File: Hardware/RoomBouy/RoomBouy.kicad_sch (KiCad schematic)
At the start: 30 parts, among them J1 Roomba Wake, J2 Raspberry_Pi_2_3, J3 Roomba Connector, J4 ProtoPad, J5 Servo, Q1 MMBT3904, Q2 MMBT3904, Q3 MMBT3906, Q4 MMBT3904, Q6 MMBT3906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

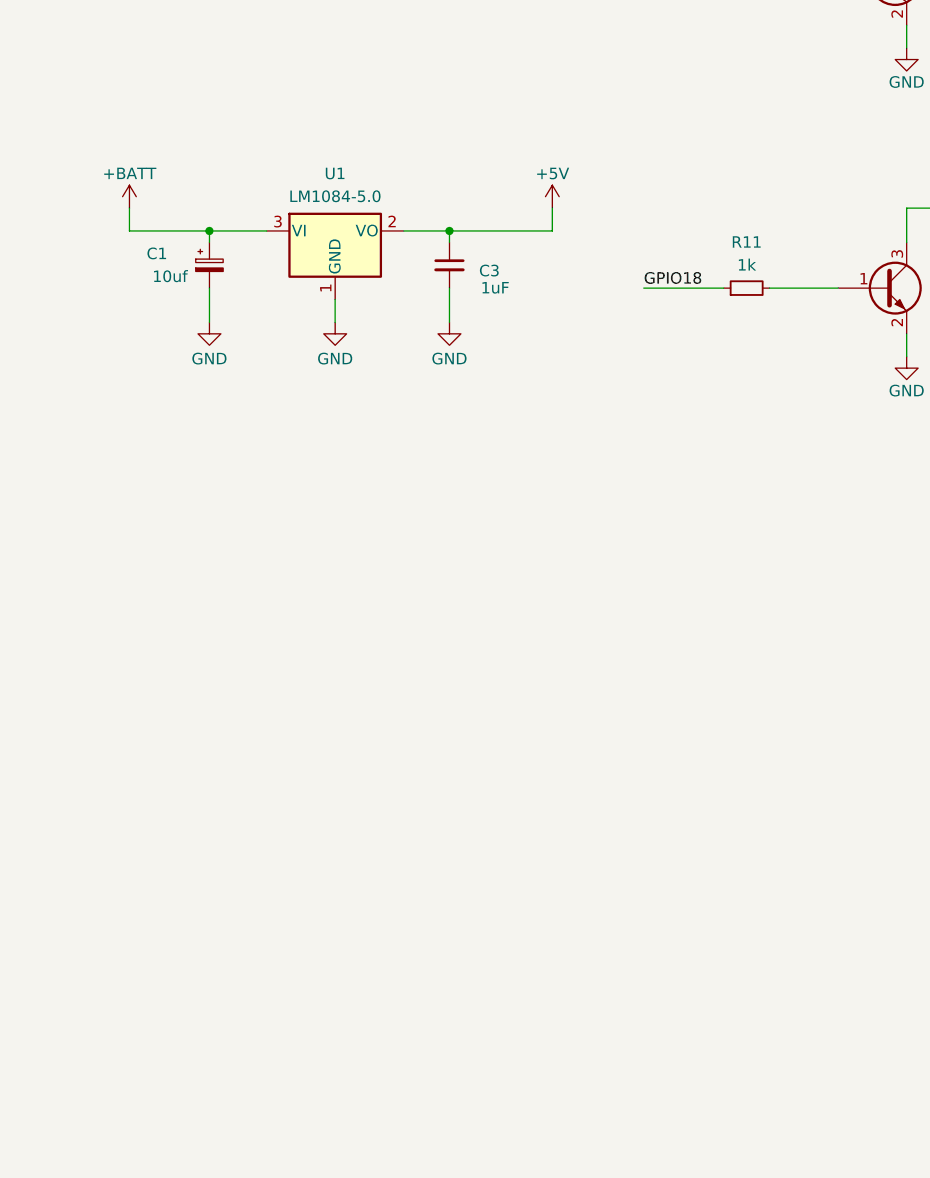
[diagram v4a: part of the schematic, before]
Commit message: Add a low-voltage protection circuit (to protect against over-discharging roomba batteries
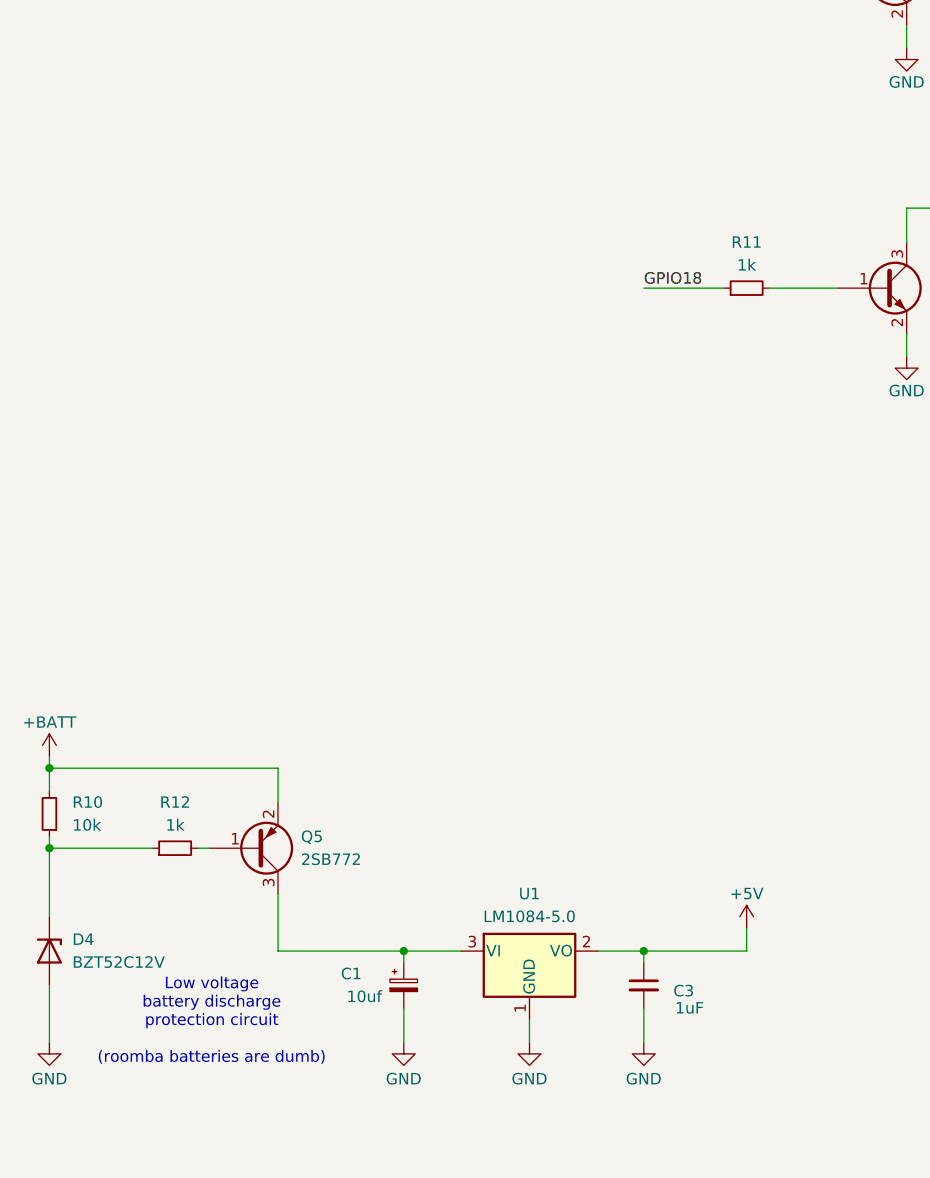
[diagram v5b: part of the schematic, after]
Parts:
- added D4: BZT52C12V, Diode_SMD:D_SOD-123, symbol Device:D_Zener
- added Q5: 2SB772, Package_TO_SOT_SMD:TO-252-2, symbol Transistor_BJT:MMBT3906
- added R10: 10k, Resistor_SMD:R_0805_2012Metric, symbol Device:R_Small
- added R12: 1k, Resistor_SMD:R_0805_2012Metric, symbol Device:R_Small
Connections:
- net +BATT: now also Q5.2 (E), R10.2; no longer C1.1, U1.3 (VI)
- net GND: now also D4.2 (A)
- new net: C1.1, Q5.3 (C), U1.3 (VI)
- new net: D4.1 (K), R10.1, R12.1
- new net: Q5.1 (B), R12.2
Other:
- note added: "Low voltage battery discharge protection circuit (roomba batteries are dumb)"
- moved on the sheet: C1, C3, U1

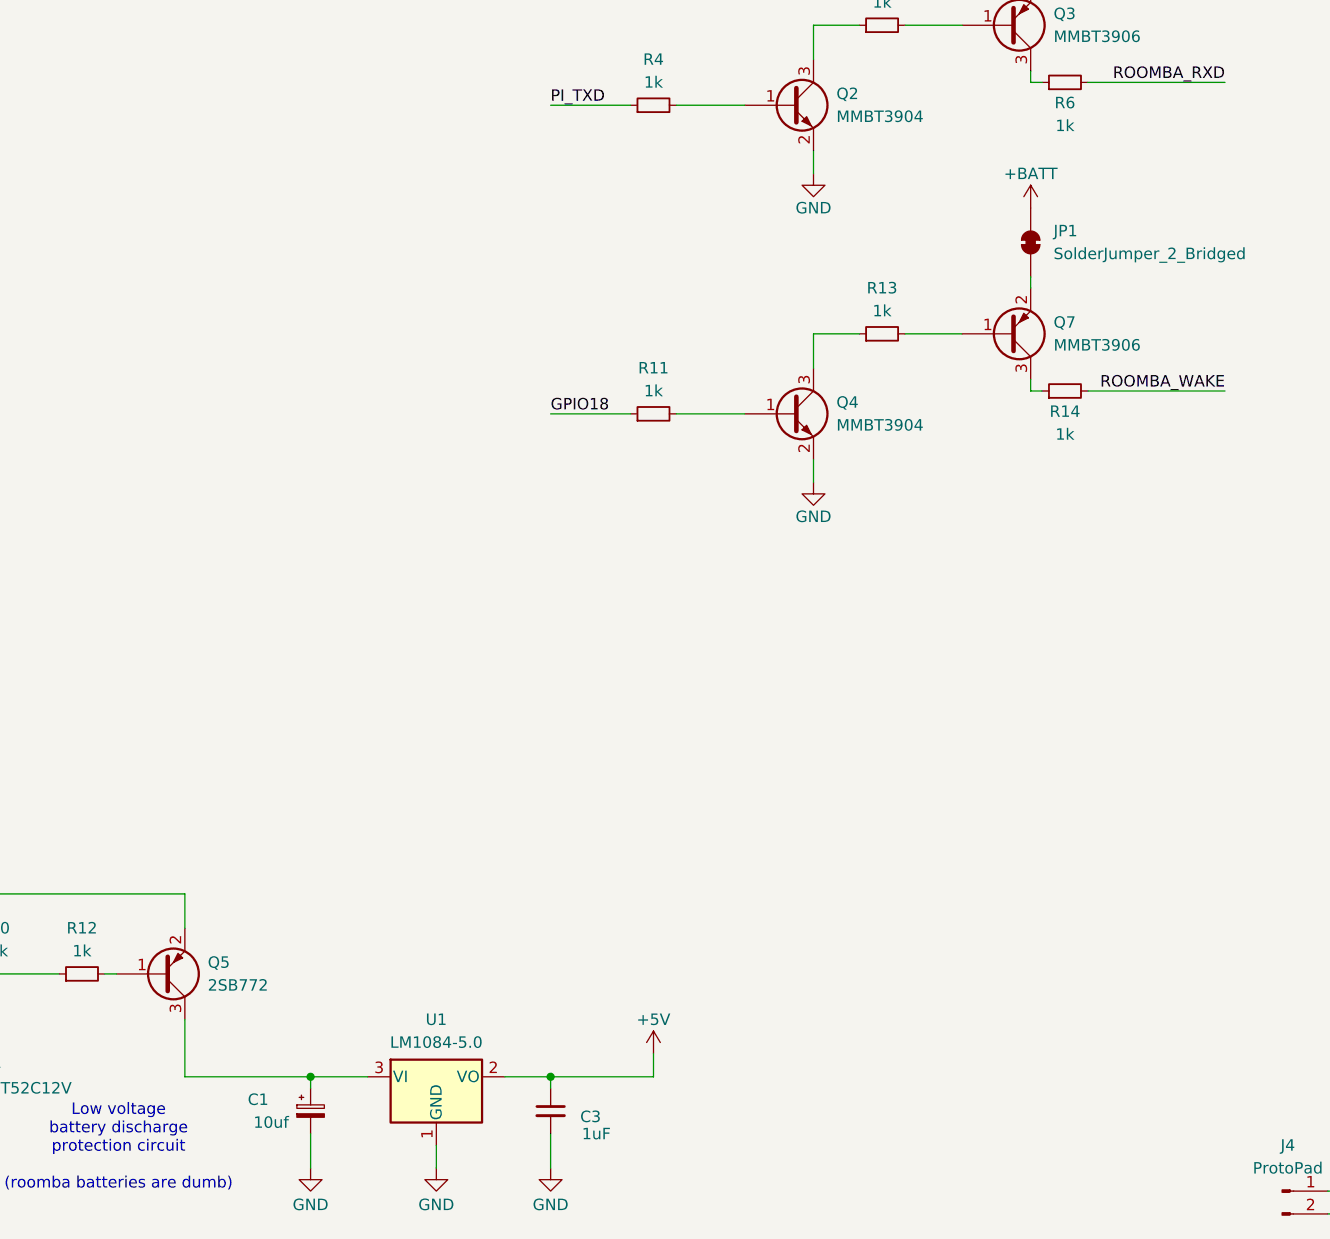
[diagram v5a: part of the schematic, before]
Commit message: Fix switched power
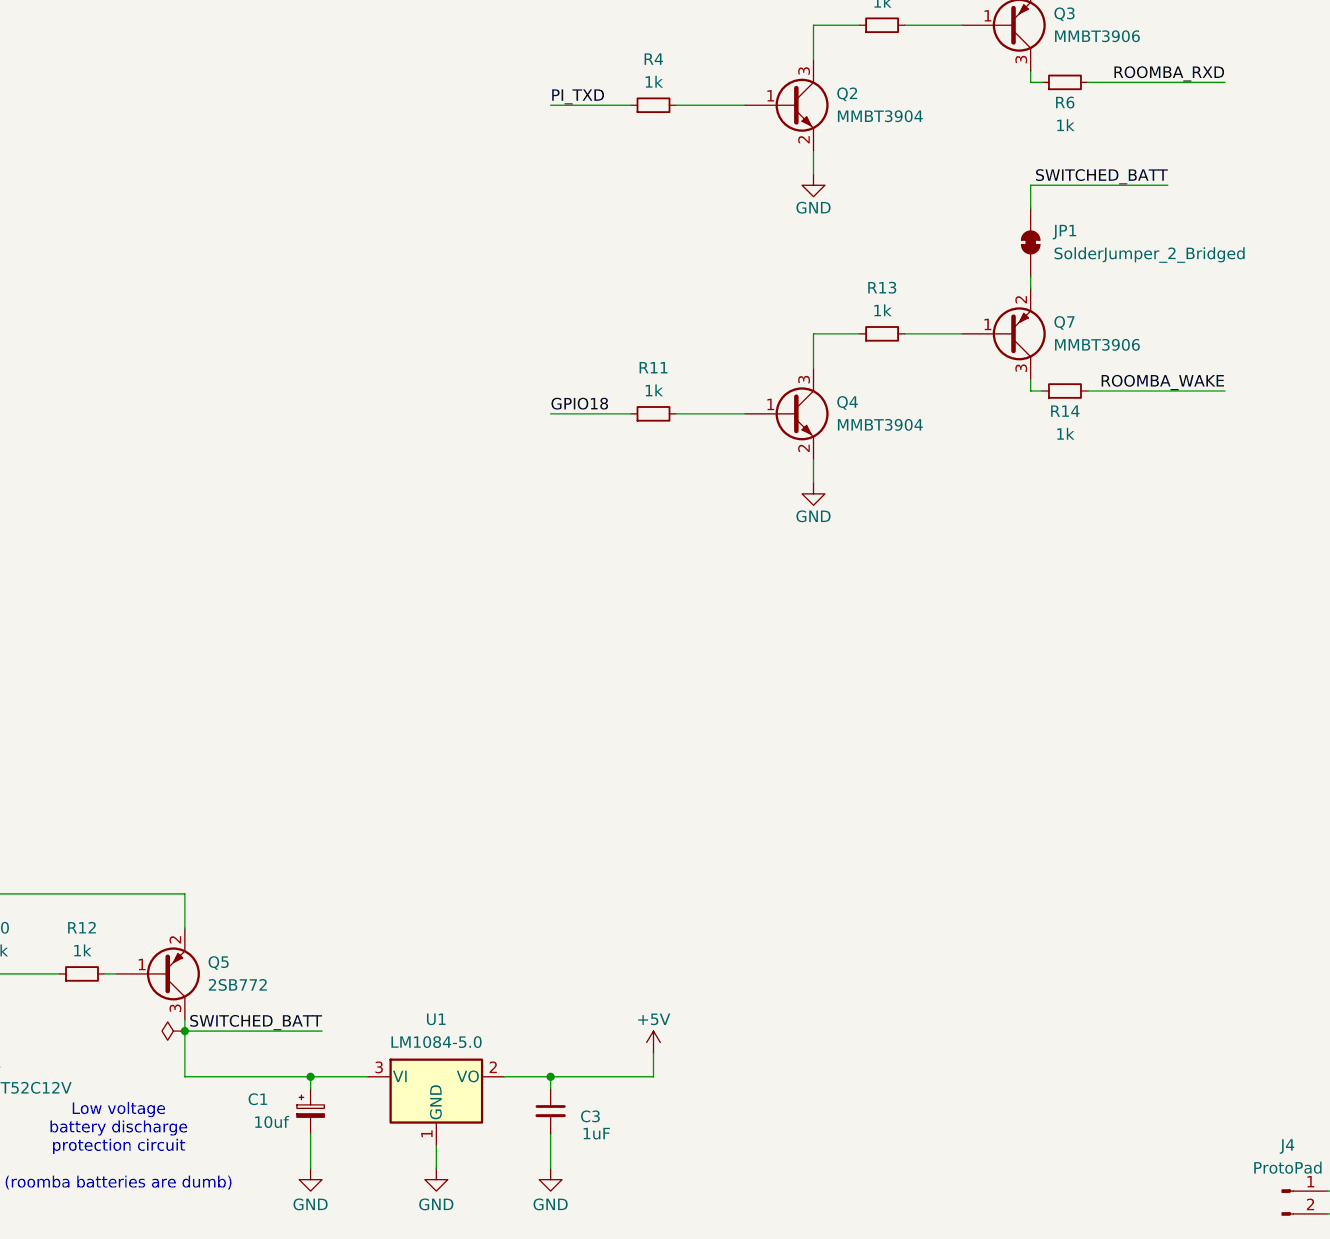
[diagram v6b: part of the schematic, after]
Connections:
- net +BATT: no longer JP1.2 (B)
- net SWITCHED_BATT: now reaches C1.1, Q5.3 (C), U1.3 (VI)
- net SWITCHED_BATT: now also JP1.2 (B)
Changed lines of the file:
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@@
 	)
 	(junction
+		(at 43.18 168.91)
+		(diameter 0)
+		(color 0 0 0 0)
+	)
+	(junction
 		(at 245.11 80.01)
 		(diameter 0)
@@
 	(wire
 		(pts
-			(xy 43.18 167.64) (xy 43.18 173.99)
+			(xy 43.18 167.64) (xy 43.18 168.91)
+		)
+		(stroke
+			(width 0)
+			(type default)
+		)
+	)
+	(wire
+		(pts
+			(xy 43.18 168.91) (xy 58.42 168.91)
 		)
 		(stroke
@@
 	(wire
 		(pts
+			(xy 137.16 74.93) (xy 137.16 77.47)
+		)
+		(stroke
+			(width 0)
+			(type default)
+		)
+	)
+	(wire
+		(pts
 			(xy 172.72 189.23) (xy 170.18 189.23)
 		)
@@
 	(wire
 		(pts
+			(xy 152.4 74.93) (xy 137.16 74.93)
+		)
+		(stroke
+			(width 0)
+			(type default)
+		)
+	)
+	(wire
+		(pts
 			(xy 113.03 71.12) (xy 113.03 73.66)
 		)
@@
 	(wire
 		(pts
+			(xy 43.18 168.91) (xy 43.18 173.99)
+		)
+		(stroke
+			(width 0)
+			(type default)
+		)
+	)
+	(wire
+		(pts
 			(xy 113.03 105.41) (xy 113.03 107.95)
 		)
@@
 		)
 	)
+	(label "SWITCHED_BATT"
+		(at 152.4 74.93 180)
+		(fields_autoplaced yes)
+		(effects
+			(font
+				(size 1.27 1.27)
+			)
+			(justify right bottom)
+		)
+	)
 	(label "PI_TXD"
 		(at 210.82 92.71 0)
@@
 		)
 	)
+	(label "SWITCHED_BATT"
+		(at 58.42 168.91 180)
+		(fields_autoplaced yes)
+		(effects
+			(font
+				(size 1.27 1.27)
+			)
+			(justify right bottom)
+		)
+	)
 	(label "ROOMBA_RXD"
 		(at 165.1 34.29 0)
@@
 	)
 	(symbol
-		(lib_id "Connector:Conn_01x03_Pin")
-		(at 276.86 73.66 180)
+		(lib_id "power:PWR_FLAG")
+		(at 43.18 168.91 90)
 		(unit 1)
 		(exclude_from_sim no)
@@
 		(dnp no)
 		(fields_autoplaced yes)
-		(property "Reference" "J5"
-			(at 278.13 72.3899 0)
+		(property "Reference" "#FLG03"
+			(at 41.275 168.91 0)
 			(effects
 				(font
 					(size 1.27 1.27)
 				)
-				(justify right)
+				(hide yes)
 			)
 		)
-		(property "Value" "Servo"
-			(at 278.13 74.9299 0)
+		(property "Value" "PWR_FLAG"
+			(at 39.37 168.9099 90)
 			(effects
 				(font
 					(size 1.27 1.27)
 				)
-				(justify right)
+				(justify left)
+				(hide yes)
 			)
 		)
-		(property "Footprint" "Connector_JST:JST_PH_S3B-PH-K_1x03_P2.00mm_Horizontal"
-			(at 276.86 73.66 0)
+		(property "Footprint" ""
+			(at 43.18 168.91 0)
 			(effects
 				(font
@@
 		)
 		(property "Datasheet" "~"
-			(at 276.86 73.66 0)
+			(at 43.18 168.91 0)
 			(effects
 				(font
@@
 			)
 		)
-		(property "Description" "Generic connector, single row, 01x03, script generated"
-			(at 276.86 73.66 0)
+		(property "Description" "Special symbol for telling ERC where power comes from"
+			(at 43.18 168.91 0)
 			(effects
 				(font
@@
 			)
 		)
-		(pin "3"
-		)
-		(pin "2"
-		)
 		(pin "1"
 		)
 		(instances
-			(project ""
+			(project "RoomBouy"
 				(path "/894f620e-3404-4a40-a2a7-513bc1d5f99b"
-					(reference "J5")
+					(reference "#FLG03")
 					(unit 1)
 				)
@@
 	)
 	(symbol
-		(lib_id "power:+BATT")
-		(at 137.16 77.47 0)
+		(lib_id "Connector:Conn_01x03_Pin")
+		(at 276.86 73.66 180)
 		(unit 1)
 		(exclude_from_sim no)
@@
 		(on_board yes)
 		(dnp no)
-		(property "Reference" "#PWR021"
-			(at 137.16 81.28 0)
+		(fields_autoplaced yes)
+		(property "Reference" "J5"
+			(at 278.13 72.3899 0)
 			(effects
 				(font
 					(size 1.27 1.27)
 				)
-				(hide yes)
+				(justify right)
 			)
 		)
-		(property "Value" "+BATT"
-			(at 137.16 73.66 0)
+		(property "Value" "Servo"
+			(at 278.13 74.9299 0)
 			(effects
 				(font
 					(size 1.27 1.27)
 				)
+				(justify right)
 			)
 		)
-		(property "Footprint" ""
-			(at 137.16 77.47 0)
+		(property "Footprint" "Connector_JST:JST_PH_S3B-PH-K_1x03_P2.00mm_Horizontal"
+			(at 276.86 73.66 0)
 			(effects
 				(font
@@
 			)
 		)
-		(property "Datasheet" ""
-			(at 137.16 77.47 0)
+		(property "Datasheet" "~"
+			(at 276.86 73.66 0)
 			(effects
 				(font
@@
 			)
 		)
-		(property "Description" "Power symbol creates a global label with name \"+BATT\""
-			(at 137.16 77.47 0)
+		(property "Description" "Generic connector, single row, 01x03, script generated"
+			(at 276.86 73.66 0)
 			(effects
 				(font
@@
 			)
 		)
+		(pin "3"
+		)
+		(pin "2"
+		)
 		(pin "1"
 		)
 		(instances
-			(project "RoomBouy"
+			(project ""
 				(path "/894f620e-3404-4a40-a2a7-513bc1d5f99b"
-					(reference "#PWR021")
+					(reference "J5")
 					(unit 1)
 				)

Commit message: Bump rpi_hat_template
Co-Authored By: @devbisme
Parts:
- J5: footprint Connector_JST:JST_PH_S3B-PH-K_1x03_P2.00mm_Horizontal -> Connector_JST:JST_EH_S3B-EH_1x03_P2.50mm_Horizontal
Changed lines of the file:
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@@
 			)
 		)
-		(property "Footprint" "Connector_JST:JST_PH_S3B-PH-K_1x03_P2.00mm_Horizontal"
+		(property "Footprint" "Connector_JST:JST_EH_S3B-EH_1x03_P2.50mm_Horizontal"
 			(at 276.86 73.66 0)
 			(effects

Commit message: Bump to new ver
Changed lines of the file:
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@@
 (kicad_sch
-	(version 20231120)
+	(version 20250114)
 	(generator "eeschema")
-	(generator_version "8.0")
+	(generator_version "9.0")
 	(paper "A4")
 	(title_block
@@
 		(company "Concord Robotics")
 	)
+	(text "Low voltage\nbattery discharge\nprotection circuit\n\n(roomba batteries are dumb)"
+		(exclude_from_sim no)
+		(at 35.814 181.864 0)
+		(effects
+			(font
+				(size 1.27 1.27)
+			)
+		)
+	)
 	(junction
 		(at 83.82 173.99)
@@
 		)
 	)
-	(text "Low voltage\nbattery discharge\nprotection circuit\n\n(roomba batteries are dumb)"
-		(exclude_from_sim no)
-		(at 35.814 181.864 0)
-		(effects
-			(font
-				(size 1.27 1.27)
-			)
-		)
-	)
 	(label "GPIO18"
 		(at 210.82 105.41 0)
-		(fields_autoplaced yes)
 		(effects
 			(font
@@
 	(label "SERVO"
 		(at 212.09 120.65 0)
-		(fields_autoplaced yes)
 		(effects
 			(font
@@
 	(label "SWITCHED_BATT"
 		(at 152.4 74.93 180)
-		(fields_autoplaced yes)
 		(effects
 			(font
@@
 	(label "PI_TXD"
 		(at 210.82 92.71 0)
-		(fields_autoplaced yes)
 		(effects
 			(font
@@
 	(label "ROOMBA_TXD"
 		(at 77.47 38.1 0)
-		(fields_autoplaced yes)
 		(effects
 			(font
@@
 	(label "ROOMBA_RXD"
 		(at 60.96 31.75 180)
-		(fields_autoplaced yes)
 		(effects
 			(font
@@
 	(label "PI_RXD"
 		(at 151.13 35.56 180)
-		(fields_autoplaced yes)
 		(effects
 			(font
@@
 	(label "ROOMBA_WAKE"
 		(at 60.96 46.99 180)
-		(fields_autoplaced yes)
 		(effects
 			(font
@@
 	(label "PI_RXD"
 		(at 210.82 95.25 0)
-		(fields_autoplaced yes)
 		(effects
 			(font
@@
 	(label "ROOMBA_TXD"
 		(at 165.1 22.86 0)
-		(fields_autoplaced yes)
 		(effects
 			(font
@@
 	(label "SWITCHED_BATT"
 		(at 58.42 168.91 180)
-		(fields_autoplaced yes)
 		(effects
 			(font
@@
 	(label "ROOMBA_RXD"
 		(at 165.1 34.29 0)
-		(fields_autoplaced yes)
 		(effects
 			(font
@@
 	(label "PI_TXD"
 		(at 83.82 66.04 0)
-		(fields_autoplaced yes)
 		(effects
 			(font
@@
 	(label "ROOMBA_TXD"
 		(at 60.96 29.21 180)
-		(fields_autoplaced yes)
 		(effects
 			(font
@@
 	(label "ROOMBA_WAKE"
 		(at 158.75 97.79 180)
-		(fields_autoplaced yes)
 		(effects
 			(font
@@
 	(label "GPIO18"
 		(at 83.82 100.33 0)
-		(fields_autoplaced yes)
 		(effects
 			(font
@@
 	(label "SERVO"
 		(at 262.89 73.66 0)
-		(fields_autoplaced yes)
 		(effects
 			(font
@@
 	(label "ROOMBA_RXD"
 		(at 158.75 63.5 180)
-		(fields_autoplaced yes)
 		(effects
 			(font
@@
 		)
 	)
+	(embedded_fonts no)
 )
